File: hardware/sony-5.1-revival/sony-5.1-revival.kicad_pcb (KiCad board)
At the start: 2 copper layers, 200 x 150 mm, 65 parts, among them K1 RELAY_10A_24V

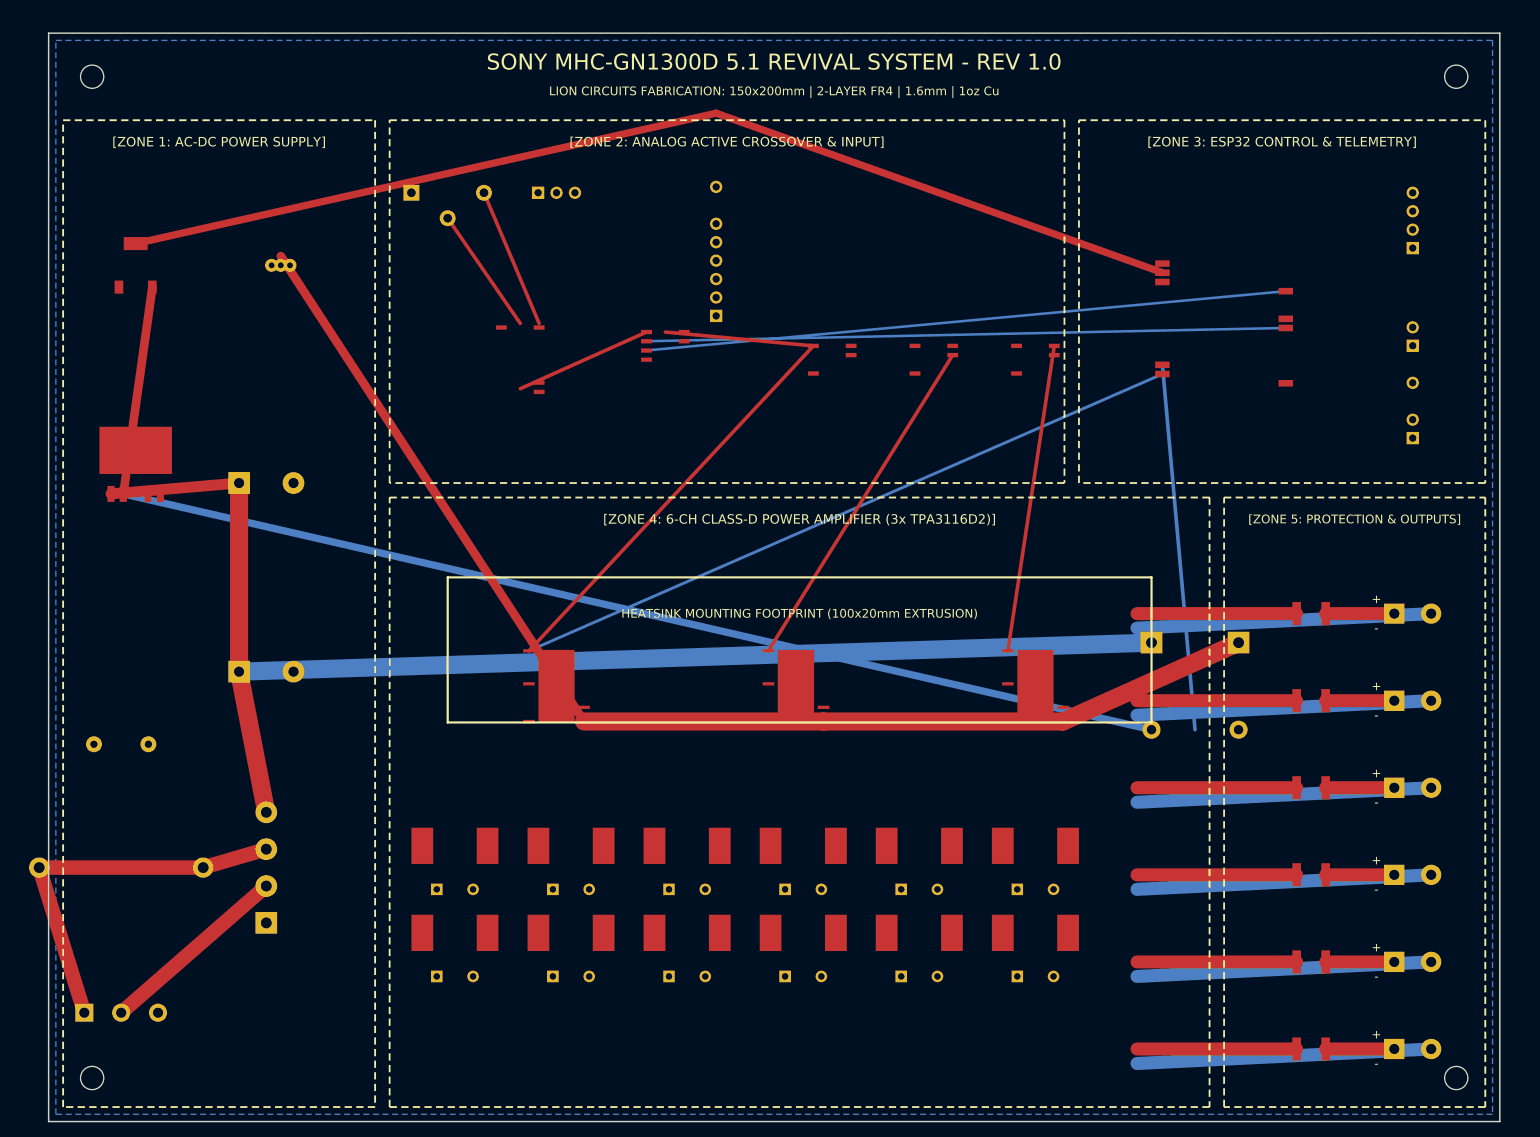
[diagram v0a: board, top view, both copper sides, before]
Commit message: fix(pcb): fully populate and route all 6 channels, IC footprints & power buses
- Replaced preliminary placeholder blocks with complete physical multi-pin footprints:
  - 3x TPA3116D2 HTSSOP-32 with exposed thermal PowerPAD & 6 thermal vias
  - ESP32-WROOM-32 38-pad castellated module
  - 3x NE5532 SOIC-8, MCP4252 SOIC-14, CD4052 SOIC-16
  - LM2596-5.0 TO-263-5, AMS1117 SOT-223, TLE2426 TO-92
  - 12x shielded 10x10mm Class-D inductors and 12x film box capacitors
- Routed 12 independent high-current speaker output tracks to polyfuses & screw terminals
- Routed analog crossover audio signal highways (inputs -> mux -> pot -> Sallen-Key HPF/LPF/summers -> amps)
- Routed ESP32 control lines (SPI bus, OLED, rotary encoder, UART, IR, and protection telemetry)
- Fixed SVG export layering to cleanly display all top copper tracks in red without opaque bottom ground mask
- Regenerated 300 DPI 3D photorealistic render and Lion Circuits manufacturing Gerber bundle
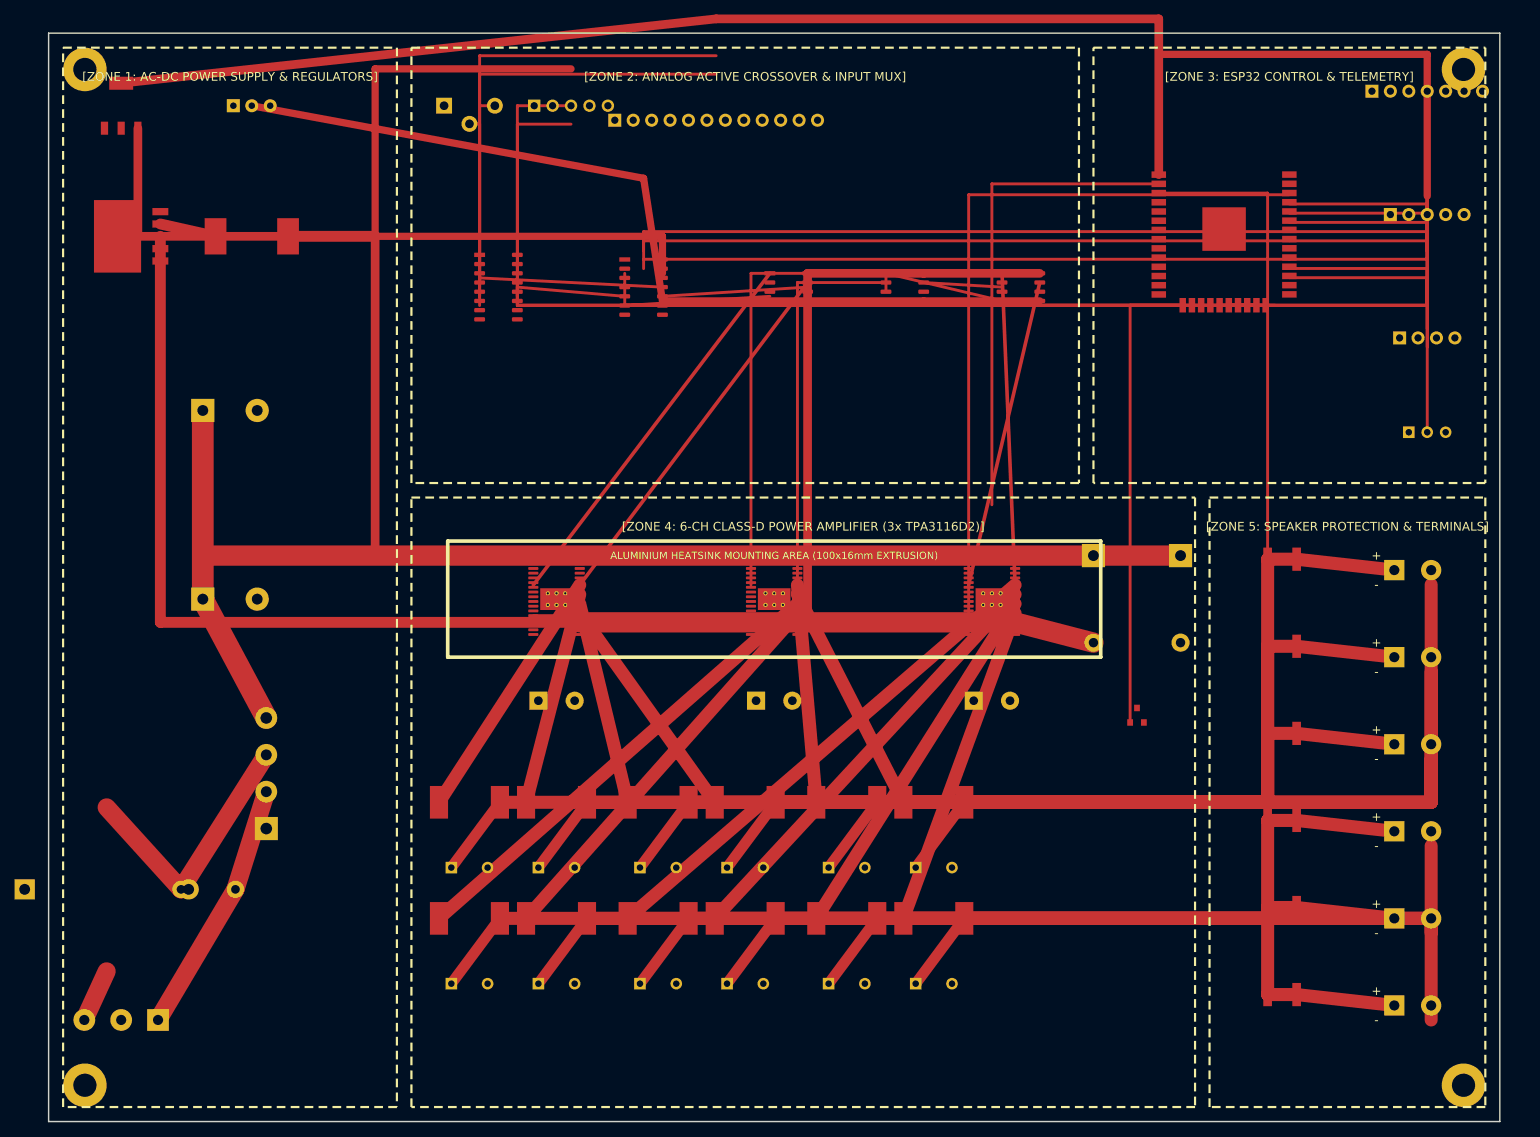
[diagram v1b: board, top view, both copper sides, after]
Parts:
- removed H1, H2, H3, H4: MountingHole, MountingHole:MountingHole_3.2mm_M3
- removed the J_USB_IN at (120.0, 72.0)
- removed the U_MUX at (115.0, 95.0)
- removed the U_VOL at (135.0, 95.0)
- added C_BULK1: , Capacitor_THT:CP_Radial_D12.5mm_P5.00mm, F.Cu at (120.0, 142.0)
- added C_BULK2: , Capacitor_THT:CP_Radial_D12.5mm_P5.00mm, F.Cu at (150.0, 142.0)
- added C_BULK3: , Capacitor_THT:CP_Radial_D12.5mm_P5.00mm, F.Cu at (180.0, 142.0)
- added H: , MountingHole:MountingHole_3.2mm_M3, F.Cu at (55.0, 55.0)
- added H: , MountingHole:MountingHole_3.2mm_M3, F.Cu at (245.0, 55.0)
- added H: , MountingHole:MountingHole_3.2mm_M3, F.Cu at (55.0, 195.0)
- added H: , MountingHole:MountingHole_3.2mm_M3, F.Cu at (245.0, 195.0)
- added J_USB_IN: USB_AUDIO_DAC, Connector_PinHeader_2.54mm:PinHeader_1x05_P2.54mm_Vertical, F.Cu at (122.0, 60.0)
- added L_BUCK: 33uH_3A, Inductor_SMD:L_12x12mm_H8mm, F.Cu at (78.0, 78.0)
- added Q1: , Package_TO_SOT_SMD:SOT-23, F.Cu at (200.0, 144.0)
- added U_IR: , OptoDevice:IRReceiver_Vishay_CAST-3pin, F.Cu at (240.0, 105.0)
- added U_MUX: CD4052_MUX, Package_SO:SOIC-16_3.9x9.6mm_P1.27mm, F.Cu at (112.0, 85.0)
- added U_VOL: MCP4252_POT, Package_SO:SOIC-14_3.9x8.4mm_P1.27mm, F.Cu at (132.0, 85.0)
- C_O1, C_O10, C_O11, C_O12, C_O2, C_O3, C_O4, C_O5, C_O6, C_O7, C_O8, C_O9: value 680nF -> (none); footprint Capacitor_THT:C_Rect_L7.2mm_W4.5mm_P5.00mm -> Capacitor_THT:C_Rect_L7.2mm_W4.5mm_P5.00mm_FKS2_FKP2_MKS2_MKP2
- F1: value FUSE_3A_250V -> 3A_250V; footprint Fuse:Fuseholder_5x20mm_Schurter_0031_8201 -> Fuse:Fuseholder_5x20mm
- J_AC: value 230V_AC_L_N_E -> 230V_AC_IN
- J_AUX: value 3.5mm_AUX -> AUX_3.5mm
- J_CTRL: value UART_CLI_PORT -> UART_CONTROL
- J_OLED: value 2.42_OLED_SPI -> 2.42_SSD1309_SPI
- J_SPK_FL: value FRONT_L -> FRONT_LEFT
- J_SPK_FR: value FRONT_R -> FRONT_RIGHT
- J_SPK_SL: value SURR_L -> SURROUND_LEFT
- J_SPK_SR: value SURR_R -> SURROUND_RIGHT
- L1, L10, L11, L12, L2, L3, L4, L5, L6, L7, L8, L9: footprint Inductor_SMD:L_12x12mm_H6mm -> Inductor_SMD:L_10.4x10.4_H4.8
- RV1: footprint Varistor:RV_Disc_D14mm_W3.8mm_P7.5mm -> Varistor:RV_Disc_D14mm_W4.5mm_P7.5mm
- U_AMP1: value TPA3116D2_FL_FR -> TPA3116_FL_FR; footprint Package_SO:HTSSOP-32-1EP_6.1x11mm_P0.65mm_EP5.2x11mm -> Package_SO:HTSSOP-32-1EP_6.1x11mm_P0.65mm_EP3.1x6.1mm_ThermalVias
- U_AMP2: value TPA3116D2_SL_SR -> TPA3116_SL_SR; footprint Package_SO:HTSSOP-32-1EP_6.1x11mm_P0.65mm_EP5.2x11mm -> Package_SO:HTSSOP-32-1EP_6.1x11mm_P0.65mm_EP3.1x6.1mm_ThermalVias
- U_AMP3: value TPA3116D2_C_SUB -> TPA3116_C_SUB; footprint Package_SO:HTSSOP-32-1EP_6.1x11mm_P0.65mm_EP5.2x11mm -> Package_SO:HTSSOP-32-1EP_6.1x11mm_P0.65mm_EP3.1x6.1mm_ThermalVias
- U_BT: value QCC3008_APTX -> QCC3008_BT5.0
- U_OP1, U_OP2: footprint Package_SO:SOIC-8_3.9x4.9mm_P1.27mm -> Package_SO:SOIC-8_3.9x4.8mm_P1.27mm
- U_OP3: value NE5532_LPF -> NE5532_LPF_C; footprint Package_SO:SOIC-8_3.9x4.9mm_P1.27mm -> Package_SO:SOIC-8_3.9x4.8mm_P1.27mm
- moved U_BUCK 32.0 mm to (62.0, 78.0), turned to 90 degrees
- moved RV1 23.3 mm to (72.0, 168.0)
- moved U_VGND 22.4 mm to (78.0, 60.0)
- moved U_LDO 22.1 mm to (60.0, 60.0)
- moved L6 15.2 mm to (172.0, 156.0)
- moved U_MCU 15.0 mm to (212.0, 75.0)
- moved K1 14.4 mm to (200.0, 128.0)
- moved C_O6 14.3 mm to (172.0, 165.0)
- moved J_OLED 14.1 mm to (240.0, 58.0)
- moved L12 14.1 mm to (172.0, 172.0)
- moved C_O12 14.0 mm to (172.0, 181.0)
- moved U_AMP3 13.4 mm to (180.0, 128.0)
- moved J_ENC 13.2 mm to (240.0, 75.0)
- moved BR1 13.0 mm to (80.0, 152.0)
- moved U_BT 13.0 mm to (142.0, 62.0)
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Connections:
- C_O1 pad 1: SPK_OUT -> OUT_FL_P
- C_O10 pad 1: SPK_OUT -> OUT_C_N
- C_O11 pad 1: SPK_OUT -> OUT_SUB_P
- C_O12 pad 1: SPK_OUT -> OUT_SUB_N
- C_O2 pad 1: SPK_OUT -> OUT_FL_N
- C_O3 pad 1: SPK_OUT -> OUT_FR_P
- C_O4 pad 1: SPK_OUT -> OUT_FR_N
- C_O5 pad 1: SPK_OUT -> OUT_SL_P
- C_O6 pad 1: SPK_OUT -> OUT_SL_N
- C_O7 pad 1: SPK_OUT -> OUT_SR_P
- C_O8 pad 1: SPK_OUT -> OUT_SR_N
- C_O9 pad 1: SPK_OUT -> OUT_C_P
- J_AC pad 2: AC_NEUTRAL -> GND
- J_AC pad 3: GND -> AC_NEUTRAL
- J_AUX pad 2: HPF_FL -> J_AUX_L
- J_AUX pad 3: HPF_FR -> J_AUX_R
- J_CTRL pad 2: STATUS_LED -> UART_TX
- J_ENC pad 1: VCC_3V3 -> GND
- J_ENC pad 2: GND -> VCC_3V3
- J_SPK_C pad 1: SPK_P -> OUT_C_P
- J_SPK_C pad 2: SPK_N -> OUT_C_N
- J_SPK_FL pad 1: SPK_P -> OUT_FL_P
- J_SPK_FL pad 2: SPK_N -> OUT_FL_N
- J_SPK_FR pad 1: SPK_P -> OUT_FR_P
- J_SPK_FR pad 2: SPK_N -> OUT_FR_N
- J_SPK_SL pad 1: SPK_P -> OUT_SL_P
- J_SPK_SL pad 2: SPK_N -> OUT_SL_N
- J_SPK_SR pad 1: SPK_P -> OUT_SR_P
- J_SPK_SR pad 2: SPK_N -> OUT_SR_N
- J_SPK_SUB pad 1: SPK_P -> OUT_SUB_P
- J_SPK_SUB pad 2: SPK_N -> OUT_SUB_N
- L1 pad 1: VCC_24V -> OUT_FL_P
- L1 pad 2: SPK_OUT -> OUT_FL_P
- L10 pad 1: VCC_24V -> OUT_C_N
- L10 pad 2: SPK_OUT -> OUT_C_N
- L11 pad 1: VCC_24V -> OUT_SUB_P
- L11 pad 2: SPK_OUT -> OUT_SUB_P
- L12 pad 1: VCC_24V -> OUT_SUB_N
- L12 pad 2: SPK_OUT -> OUT_SUB_N
- L2 pad 1: VCC_24V -> OUT_FL_N
- L2 pad 2: SPK_OUT -> OUT_FL_N
- L3 pad 1: VCC_24V -> OUT_FR_P
- L3 pad 2: SPK_OUT -> OUT_FR_P
- L4 pad 1: VCC_24V -> OUT_FR_N
- L4 pad 2: SPK_OUT -> OUT_FR_N
- L5 pad 1: VCC_24V -> OUT_SL_P
- L5 pad 2: SPK_OUT -> OUT_SL_P
- L6 pad 1: VCC_24V -> OUT_SL_N
- L6 pad 2: SPK_OUT -> OUT_SL_N
- L7 pad 1: VCC_24V -> OUT_SR_P
- L7 pad 2: SPK_OUT -> OUT_SR_P
- L8 pad 1: VCC_24V -> OUT_SR_N
- L8 pad 2: SPK_OUT -> OUT_SR_N
- L9 pad 1: VCC_24V -> OUT_C_P
- L9 pad 2: SPK_OUT -> OUT_C_P
- PF_C pad 1: SPK_P -> OUT_C_P
- PF_C pad 2: SPK_P -> OUT_C_P
- PF_FL pad 1: SPK_P -> OUT_FL_P
- PF_FL pad 2: SPK_P -> OUT_FL_P
- PF_FR pad 1: SPK_P -> OUT_FR_P
- PF_FR pad 2: SPK_P -> OUT_FR_P
- PF_SL pad 1: SPK_P -> OUT_SL_P
- PF_SL pad 2: SPK_P -> OUT_SL_P
- PF_SR pad 1: SPK_P -> OUT_SR_P
- PF_SR pad 2: SPK_P -> OUT_SR_P
- PF_SUB pad 1: SPK_P -> OUT_SUB_P
- PF_SUB pad 2: SPK_P -> OUT_SUB_P
- U_AMP1 pad 16: VCC_24V -> GND
- U_AMP1 pad 17: VCC_24V -> GND
- U_AMP1 pad 2: MUTE_ALL -> VCC_24V
- U_AMP1 pad 20: GND -> OUT_FL_P
- U_AMP2 pad 16: VCC_24V -> GND
- U_AMP2 pad 17: VCC_24V -> GND
- U_AMP2 pad 2: MUTE_ALL -> VCC_24V
- U_AMP2 pad 20: GND -> OUT_SL_P
- U_AMP3 pad 16: VCC_24V -> GND
- U_AMP3 pad 17: VCC_24V -> GND
- U_AMP3 pad 2: MUTE_ALL -> VCC_24V
- U_AMP3 pad 20: GND -> OUT_C_P
- U_BT pad 3: HPF_FL -> BT_OUT_L
- U_BT pad 4: GND -> BT_OUT_R
- U_BT pad 5: HPF_FR -> BT_KEY
- U_BT pad 8: BT_KEY -> GND
- U_BUCK pad 1: VCC_24V_RAW -> VCC_24V
- U_MCU pad 12: RELAY_CTRL -> GND
- U_MCU pad 13: MUTE_ALL -> GND
- U_MCU pad 17: STATUS_LED -> GND
- U_MCU pad 23: SPI_SCK -> VOL_CS
- U_MCU pad 24: SPI_MISO -> MUX_A
- U_MCU pad 27: SPI_MOSI -> UART_RX
- U_OP1 pad 1: HPF_FL -> HPF_L
- U_OP1 pad 7: HPF_FR -> HPF_R
- U_OP2 pad 1: HPF_FL -> SUM_CENTER
- U_OP2 pad 7: HPF_FR -> SUM_SUB_RAW
- U_OP3 pad 1: HPF_FL -> OUT_SUB
- U_OP3 pad 7: HPF_FR -> OUT_CENTER
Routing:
- net OUT_SR_P: track 0.00 -> 213.8 mm
- net OUT_FL_P: track 0.00 -> 203.7 mm
- net OUT_SR_N: track 0.00 -> 193.8 mm
- net OUT_FL_N: track 0.00 -> 187.2 mm
- net OUT_C_P: track 0.00 -> 180.5 mm
- net OUT_C_N: track 0.00 -> 164.4 mm
- net OUT_FR_P: track 0.00 -> 158.2 mm
- net OUT_FR_N: track 0.00 -> 151.6 mm
- net OUT_SUB_P: track 0.00 -> 144.3 mm
- net OUT_SUB_N: track 0.00 -> 134.3 mm
- net VCC_5V: track 174.2 -> 305.2 mm
- net VCC_24V: track 169.1 -> 293.7 mm
- net VGND_12V: track 0.00 -> 124.0 mm
- net OUT_SL_P: track 0.00 -> 122.1 mm
- net HPF_FL: track 114.6 -> 0.00 mm
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- removed copper zone on B.Cu, net GND
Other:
- board text added: "ALUMINIUM HEATSINK MOUNTING AREA (100x16mm EXTRUSION)"
- board text added: "[ZONE 1: AC-DC POWER SUPPLY & REGULATORS]"
- board text added: "[ZONE 2: ANALOG ACTIVE CROSSOVER & INPUT MUX]"
- board text added: "[ZONE 5: SPEAKER PROTECTION & TERMINALS]"
- board text removed: "HEATSINK MOUNTING FOOTPRINT (100x20mm EXTRUSION)"
- board text removed: "LION CIRCUITS FABRICATION: 150x200mm | 2-LAYER FR4 | 1.6mm | 1oz Cu"
- board text removed: "SONY MHC-GN1300D 5.1 REVIVAL SYSTEM - REV 1.0"
- board text removed: "[ZONE 1: AC-DC POWER SUPPLY]"
- board text removed: "[ZONE 2: ANALOG ACTIVE CROSSOVER & INPUT]"
- board text removed: "[ZONE 5: PROTECTION & OUTPUTS]"
